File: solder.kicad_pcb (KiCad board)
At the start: 2 copper layers, 53 x 36 mm, 17 parts, among them M1 Motor_DC, SW1 SW_Push, SW2 SW_Push

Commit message: added routing
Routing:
- net Net-(BT1-+): track 0.00 -> 77.4 mm
- net Net-(BT1--): track 0.00 -> 46.0 mm
- net Net-(D1-A): track 0.00 -> 38.0 mm
- net Net-(D1-K): track 0.00 -> 23.3 mm
- net Net-(M1--): track 0.00 -> 20.8 mm
- net Net-(D2-K): track 0.00 -> 6.89 mm

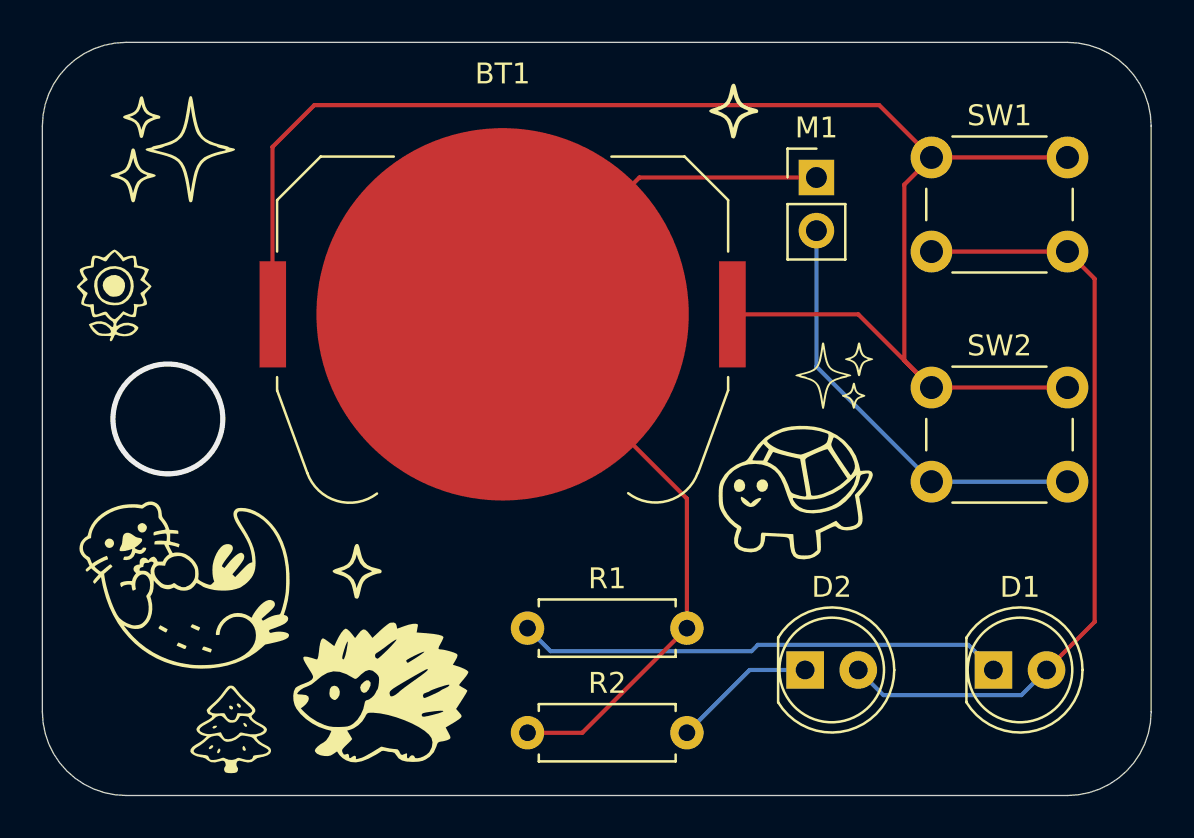
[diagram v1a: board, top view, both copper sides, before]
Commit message: rotated motor
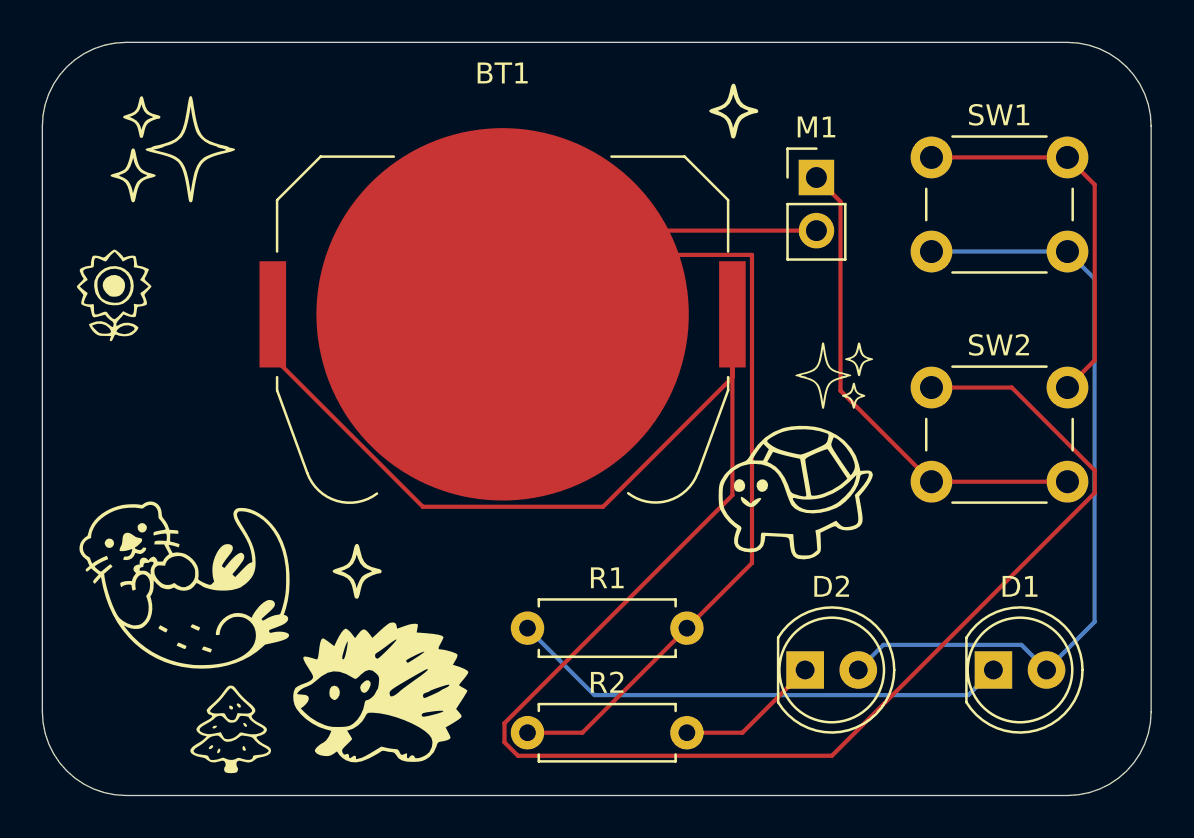
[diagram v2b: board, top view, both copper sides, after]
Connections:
- M1 pad 1: Net-(BT1--) -> Net-(M1-+)
- M1 pad 2: Net-(M1--) -> Net-(BT1--)
- SW2 pad 2: Net-(M1--) -> Net-(M1-+)
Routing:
- net Net-(BT1-+): track 77.4 -> 120.3 mm
- net Net-(M1-+): track 0.00 -> 23.3 mm
- net Net-(M1--): track 20.8 -> 0.00 mm
- net Net-(BT1--): track 46.0 -> 58.6 mm
- net Net-(D1-K): track 23.3 -> 24.1 mm
- net (no net): vias 1 -> 0
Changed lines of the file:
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@@
 	(net 4 "Net-(D2-K)")
 	(net 5 "Net-(D1-A)")
-	(net 6 "Net-(M1--)")
+	(net 6 "Net-(M1-+)")
 	(footprint "LOGO"
 		(layer "F.Cu")
@@
 			(layers "*.Cu" "*.Mask")
 			(remove_unused_layers no)
-			(net 2 "Net-(BT1--)")
+			(net 6 "Net-(M1-+)")
 			(pinfunction "+")
 			(pintype "passive")
@@
 			(layers "*.Cu" "*.Mask")
 			(remove_unused_layers no)
-			(net 6 "Net-(M1--)")
+			(net 2 "Net-(BT1--)")
 			(pinfunction "-")
 			(pintype "passive")
@@
 			(layers "*.Cu" "*.Mask")
 			(remove_unused_layers no)
-			(net 6 "Net-(M1--)")
+			(net 6 "Net-(M1-+)")
 			(pinfunction "2")
 			(pintype "passive")
@@
 			(layers "*.Cu" "*.Mask")
 			(remove_unused_layers no)
-			(net 6 "Net-(M1--)")
+			(net 6 "Net-(M1-+)")
 			(pinfunction "2")
 			(pintype "passive")
@@
 		(layer "Edge.Cuts")
 	)
-	(via
-		(at 60 65)
-		(size 5.5)
-		(drill 5)
-		(layers "F.Cu" "B.Cu")
-		(net 0)
+	(segment
+		(start 65.015 62.027179)
+		(end 72.188821 69.201)
+		(width 0.2)
+		(layer "F.Cu")
+		(net 1)
 	)
 	(segment
-		(start 93 60)
-		(end 96.5 63.5)
+		(start 76.089 80.45605)
+		(end 76.089 79.54395)
 		(width 0.2)
 		(layer "F.Cu")
@@
 	)
 	(segment
-		(start 65 52)
-		(end 67 50)
+		(start 104.301 53.801)
+		(end 103 52.5)
 		(width 0.2)
 		(layer "F.Cu")
@@
 	)
 	(segment
-		(start 96.5 52.5)
-		(end 95.199 53.801)
+		(start 76.73395 81.101)
+		(end 76.089 80.45605)
 		(width 0.2)
 		(layer "F.Cu")
@@
 	)
 	(segment
-		(start 65.015 60)
-		(end 65 59.985)
+		(start 96.5 63.5)
+		(end 100.339892 63.5)
 		(width 0.2)
 		(layer "F.Cu")
@@
 	)
 	(segment
-		(start 103 63.5)
-		(end 96.5 63.5)
+		(start 72.188821 69.201)
+		(end 80.799 69.201)
+		(width 0.2)
+		(layer "F.Cu")
+		(net 1)
+	)
+	(segment
+		(start 86.985 63.015)
+		(end 86.985 60)
 		(width 0.2)
 		(layer "F.Cu")
@@
 	)
 	(segment
-		(start 65 59.985)
-		(end 65 52)
+		(start 76.089 79.54395)
+		(end 86.985 68.64795)
 		(width 0.2)
 		(layer "F.Cu")
@@
 	)
 	(segment
-		(start 94 50)
+		(start 80.799 69.201)
+		(end 86.985 63.015)
+		(width 0.2)
+		(layer "F.Cu")
+		(net 1)
+	)
+	(segment
+		(start 91.738892 81.101)
+		(end 76.73395 81.101)
+		(width 0.2)
+		(layer "F.Cu")
+		(net 1)
+	)
+	(segment
+		(start 103 52.5)
 		(end 96.5 52.5)
 		(width 0.2)
@@
 	)
 	(segment
-		(start 86.985 60)
-		(end 93 60)
+		(start 86.985 68.64795)
+		(end 86.985 60)
 		(width 0.2)
 		(layer "F.Cu")
@@
 	)
 	(segment
-		(start 96.5 52.5)
-		(end 103 52.5)
+		(start 104.301 62.199)
+		(end 104.301 53.801)
+		(width 0.2)
+		(layer "F.Cu")
+		(net 1)
+	)
+	(segment
+		(start 65.015 60)
+		(end 65.015 62.027179)
 		(width 0.2)
 		(layer "F.Cu")
@@
 	)
 	(segment
-		(start 67 50)
-		(end 94 50)
+		(start 103 63.5)
+		(end 104.301 62.199)
 		(width 0.2)
 		(layer "F.Cu")
@@
 	)
 	(segment
-		(start 95.199 53.801)
-		(end 95.199 62.199)
+		(start 104.301 67.461108)
+		(end 104.301 68.538892)
 		(width 0.2)
 		(layer "F.Cu")
@@
 	)
 	(segment
-		(start 95.199 62.199)
-		(end 96.5 63.5)
+		(start 104.301 68.538892)
+		(end 91.738892 81.101)
 		(width 0.2)
 		(layer "F.Cu")
@@
 	)
 	(segment
-		(start 77.19 80)
-		(end 79.81 80)
+		(start 100.339892 63.5)
+		(end 104.301 67.461108)
+		(width 0.2)
+		(layer "F.Cu")
+		(net 1)
+	)
+	(segment
+		(start 91 56)
+		(end 80 56)
 		(width 0.2)
 		(layer "F.Cu")
@@
 	)
 	(segment
-		(start 91 53.46)
-		(end 82.54 53.46)
+		(start 80 56)
+		(end 76 60)
 		(width 0.2)
 		(layer "F.Cu")
@@
 	)
 	(segment
-		(start 84.81 75)
-		(end 84.81 68.81)
+		(start 78.841 57.159)
+		(end 76 60)
 		(width 0.2)
 		(layer "F.Cu")
@@
 	)
 	(segment
-		(start 82.54 53.46)
-		(end 76 60)
+		(start 84.81 75)
+		(end 87.921 71.889)
 		(width 0.2)
 		(layer "F.Cu")
@@
 	)
 	(segment
-		(start 84.81 68.81)
-		(end 76 60)
+		(start 87.921 71.889)
+		(end 87.921 57.159)
 		(width 0.2)
 		(layer "F.Cu")
@@
 	)
 	(segment
-		(start 98.259 75.799)
-		(end 99.46 77)
+		(start 87.921 57.159)
+		(end 78.841 57.159)
 		(width 0.2)
-		(layer "B.Cu")
-		(net 3)
+		(layer "F.Cu")
+		(net 2)
 	)
 	(segment
-		(start 87.899 76.101)
-		(end 88.201 75.799)
+		(start 77.19 80)
+		(end 79.81 80)
 		(width 0.2)
-		(layer "B.Cu")
-		(net 3)
+		(layer "F.Cu")
+		(net 2)
 	)
 	(segment
-		(start 77.19 75)
-		(end 78.291 76.101)
+		(start 80.391 78.201)
+		(end 98.259 78.201)
 		(width 0.2)
 		(layer "B.Cu")
@@
 	)
 	(segment
-		(start 88.201 75.799)
-		(end 98.259 75.799)
+		(start 77.19 75)
+		(end 80.391 78.201)
 		(width 0.2)
 		(layer "B.Cu")
@@
 	)
 	(segment
-		(start 78.291 76.101)
-		(end 87.899 76.101)
+		(start 98.259 78.201)
+		(end 99.46 77)
 		(width 0.2)
 		(layer "B.Cu")
@@
 	)
 	(segment
-		(start 90.46 77)
-		(end 87.81 77)
+		(start 84.81 80)
+		(end 87.46 80)
 		(width 0.2)
-		(layer "B.Cu")
+		(layer "F.Cu")
 		(net 4)
 	)
 	(segment
-		(start 87.81 77)
-		(end 84.81 80)
+		(start 87.46 80)
+		(end 90.46 77)
 		(width 0.2)
-		(layer "B.Cu")
+		(layer "F.Cu")
 		(net 4)
 	)
 	(segment
 		(start 102 77)
-		(end 104.301 74.699)
+		(end 100.799 75.799)
 		(width 0.2)
-		(layer "F.Cu")
-		(net 5)
-	)
-	(segment
-		(start 104.301 74.699)
-		(end 104.301 58.301)
-		(width 0.2)
-		(layer "F.Cu")
+		(layer "B.Cu")
 		(net 5)
 	)
@@
 		(end 103 57)
 		(width 0.2)
-		(layer "F.Cu")
+		(layer "B.Cu")
 		(net 5)
 	)
@@
 		(end 96.5 57)
 		(width 0.2)
-		(layer "F.Cu")
+		(layer "B.Cu")
 		(net 5)
 	)
 	(segment
-		(start 93 77)
-		(end 94.201 78.201)
+		(start 104.301 74.699)
+		(end 104.301 58.301)
 		(width 0.2)
 		(layer "B.Cu")
@@
 	)
 	(segment
-		(start 94.201 78.201)
-		(end 100.799 78.201)
+		(start 94.201 75.799)
+		(end 93 77)
 		(width 0.2)
 		(layer "B.Cu")
@@
 	)
 	(segment
-		(start 100.799 78.201)
-		(end 102 77)
+		(start 102 77)
+		(end 104.301 74.699)
 		(width 0.2)
 		(layer "B.Cu")
@@
 	)
 	(segment
-		(start 96.5 68)
-		(end 103 68)
+		(start 100.799 75.799)
+		(end 94.201 75.799)
 		(width 0.2)
 		(layer "B.Cu")
+		(net 5)
+	)
+	(segment
+		(start 91 53.46)
+		(end 92.151 54.611)
+		(width 0.2)
+		(layer "F.Cu")
 		(net 6)
 	)
 	(segment
-		(start 91 62.5)
+		(start 92.151 63.651)
 		(end 96.5 68)
 		(width 0.2)
-		(layer "B.Cu")
+		(layer "F.Cu")
 		(net 6)
 	)
 	(segment
-		(start 91 56)
-		(end 91 62.5)
+		(start 92.151 54.611)
+		(end 92.151 63.651)
 		(width 0.2)
-		(layer "B.Cu")
+		(layer "F.Cu")
+		(net 6)
+	)
+	(segment
+		(start 96.5 68)
+		(end 103 68)
+		(width 0.2)
+		(layer "F.Cu")
 		(net 6)
 	)
